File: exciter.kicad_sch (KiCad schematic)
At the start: 37 parts, among them U7 CC1200, X1 40MHz

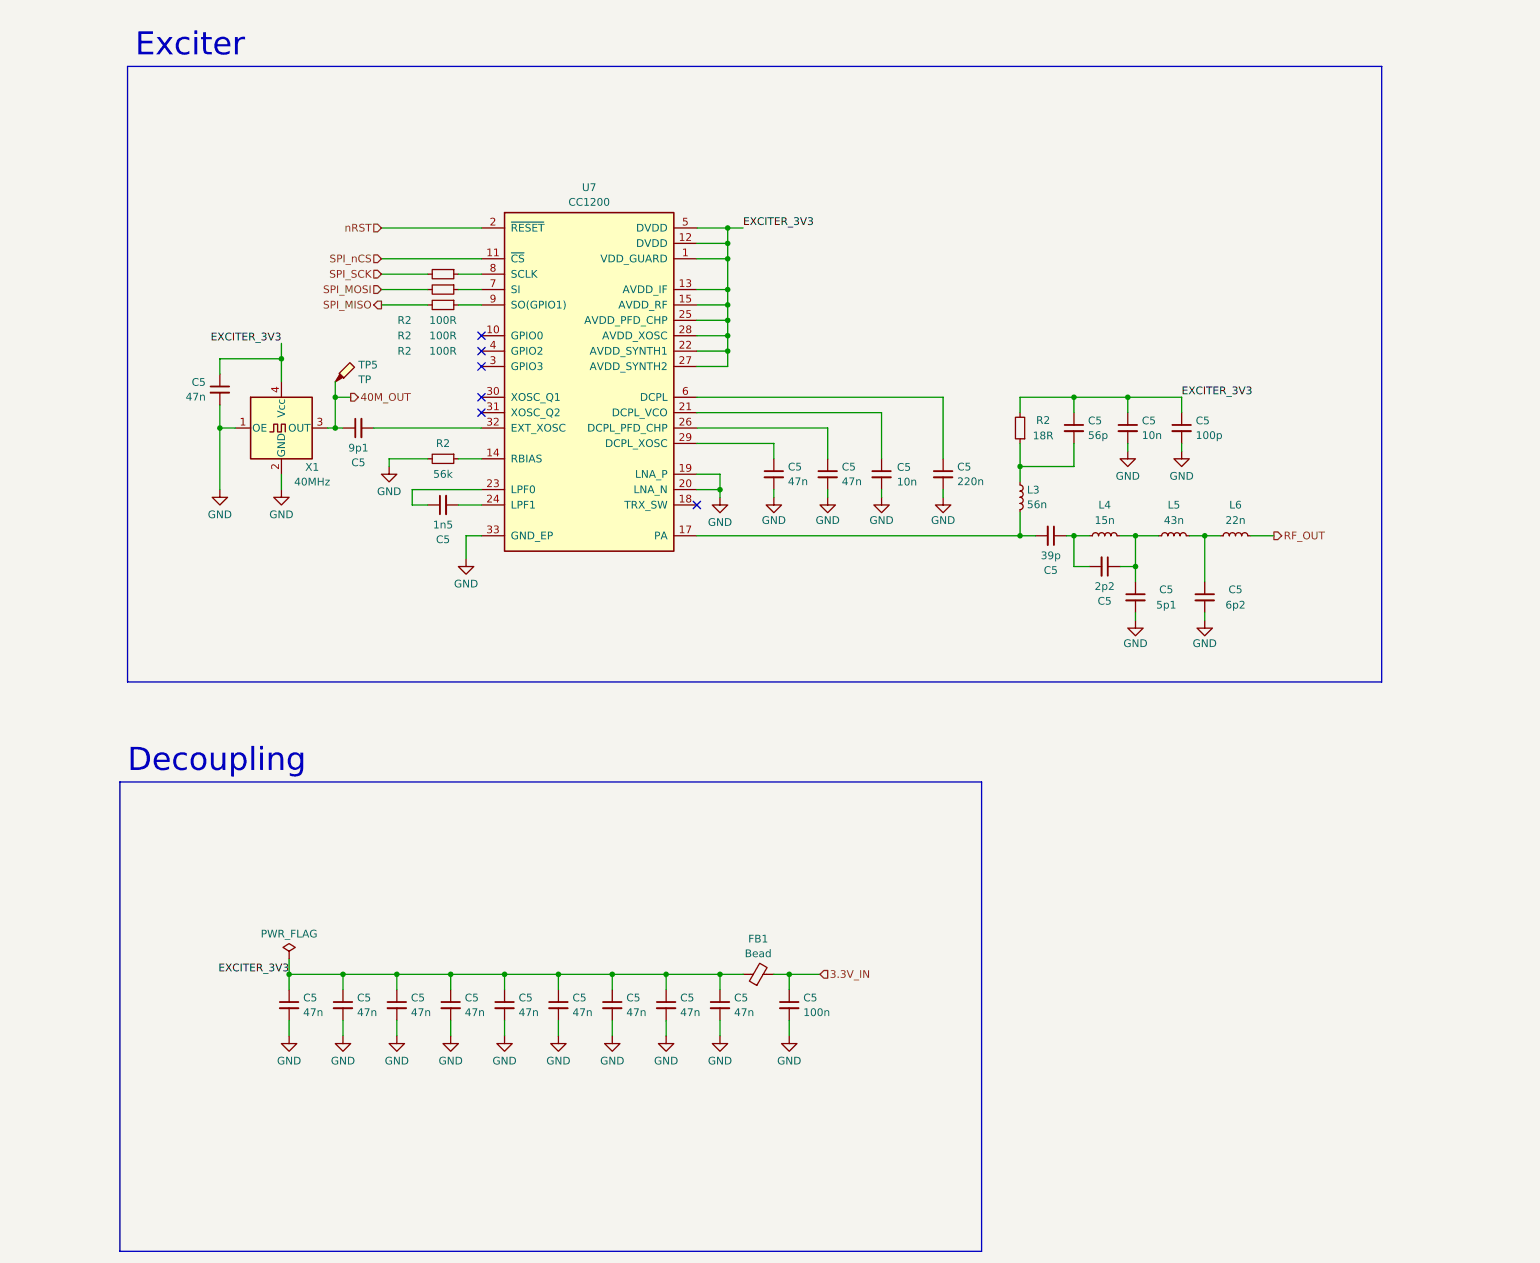
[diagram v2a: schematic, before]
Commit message: WIP rev B
- replaced R44-R46 with 22k
- exposed BOOT0 at the DA15 connector
- added a testpoint at DAC OUT2
- added a buffer to the 40MHz reference oscillator
- removed C2
- bypassed R5 with a 100nF capacitor
- changed D5's voltage to 5.1V
- routed TX_SAMP_CLK
- changed temperature sensor's supply voltage to 5V
- added a series of 100p, 1n and 10n capacitors at PA_VGG
- reduced N-connector cutouts to 2.5mm
- improved RF output track a little
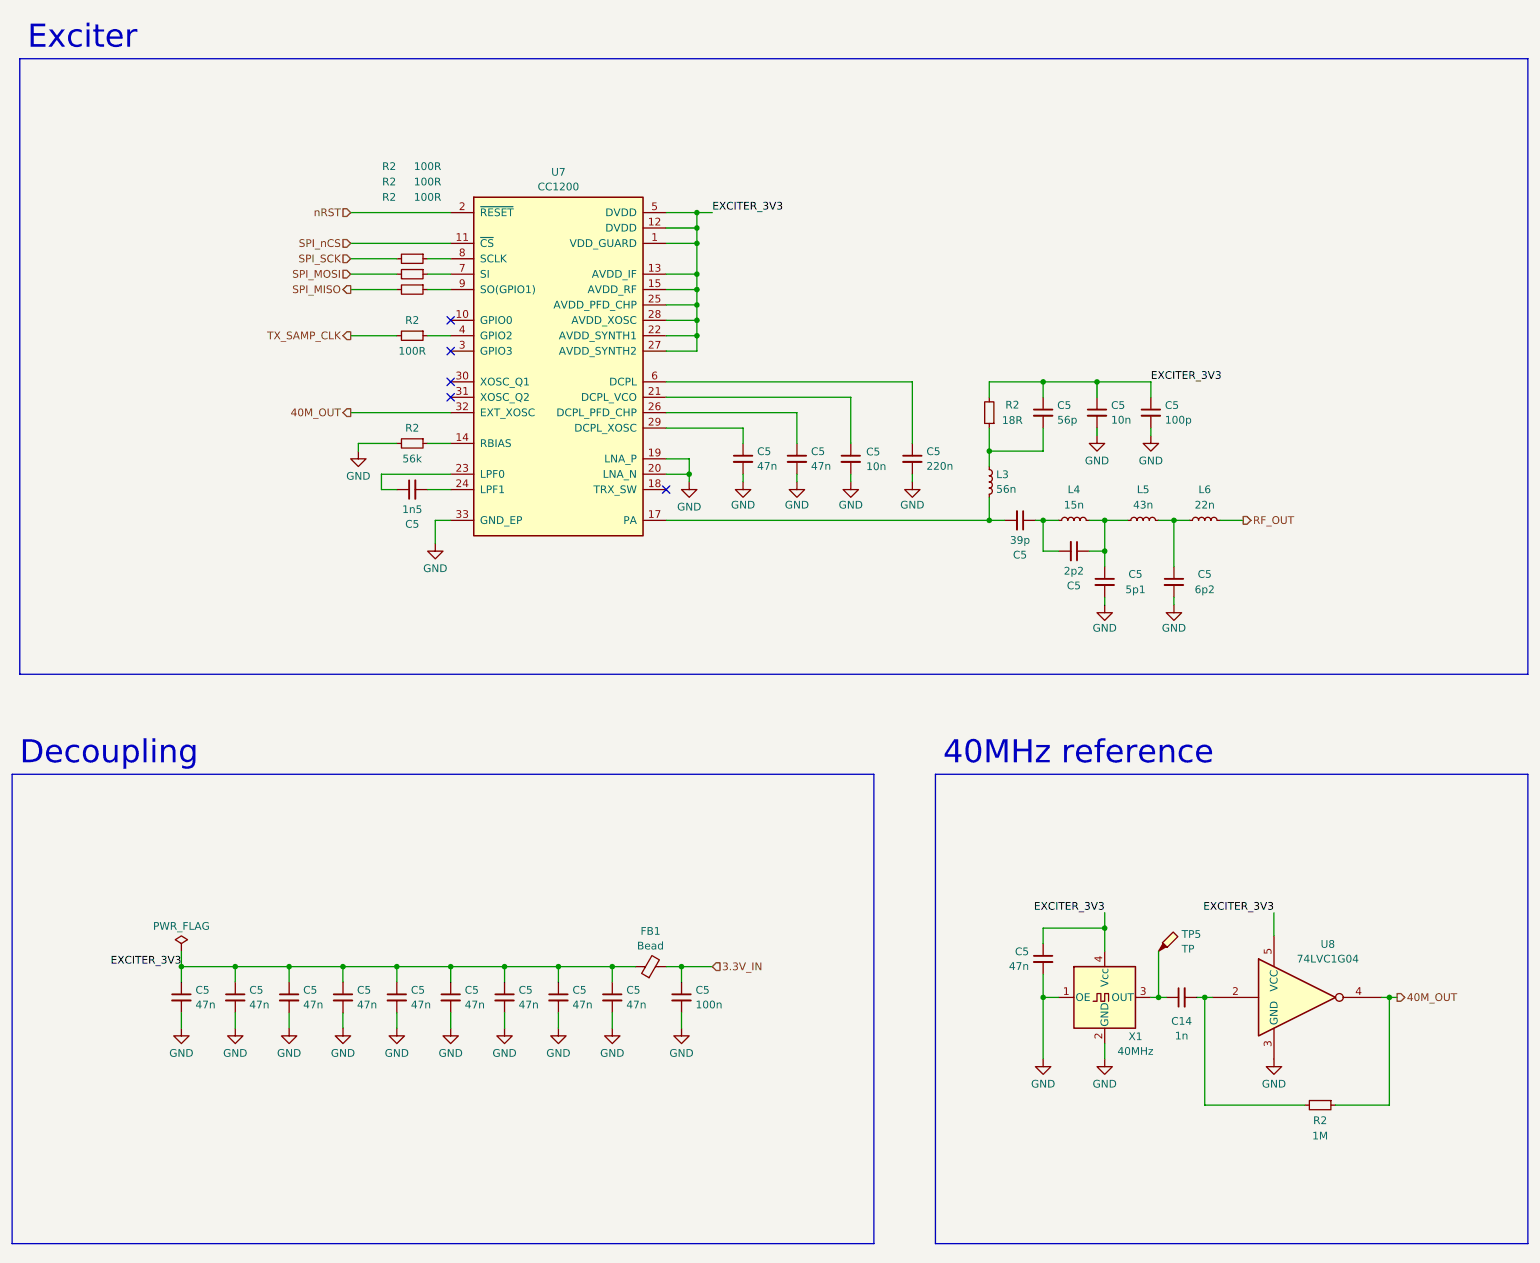
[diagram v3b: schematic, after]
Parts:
- removed C5: 9p1, Capacitor_SMD:C_0603_1608Metric, symbol Device:C_Small
- added C14: 1n, Capacitor_SMD:C_0603_1608Metric, symbol Device:C_Small
- added R2: 100R, Resistor_SMD:R_0603_1608Metric, symbol Device:R_Small
- added R2: 1M, Resistor_SMD:R_0603_1608Metric, symbol Device:R_Small
- added U8: 74LVC1G04, Package_TO_SOT_SMD:SOT-23-5, symbol 74xGxx:74LVC1G04
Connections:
- net 40M_OUT: now also U7.32 (EXT_XOSC), R2.1, U8.4; no longer TP5.1, X1.3 (OUT)
- net EXCITER_3V3: now also U8.5 (VCC)
- net GND: now also U8.3 (GND)
- net at U7.4 (GPIO2): now also R2.1
- new net: C14.1, TP5.1, X1.3 (OUT)
- new net: C14.2, R2.2, U8.2
- new net TX_SAMP_CLK: R2.2
- no-connect marks 6 -> 5
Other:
- note added: "40MHz reference"
- moved on the sheet: C5, FB1, L3, L4, L5, L6, R2, TP5, U7, X1

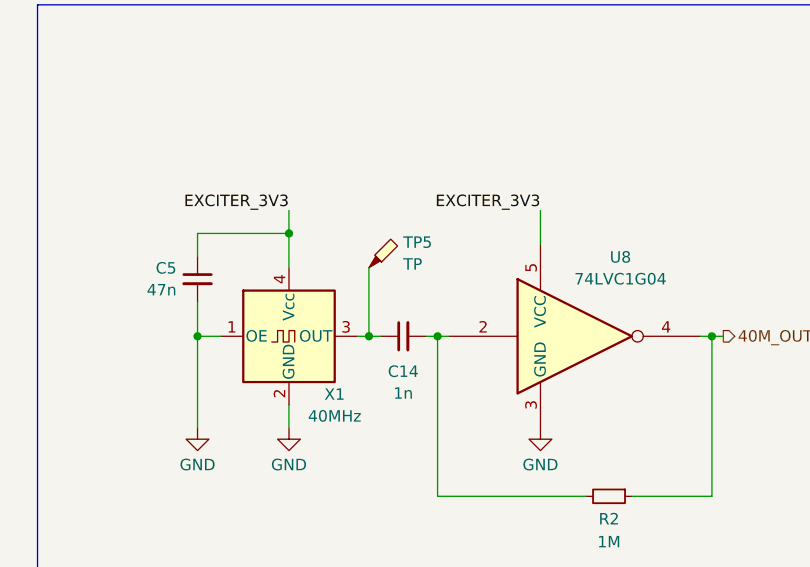
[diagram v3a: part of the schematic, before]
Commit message: routed the 40MHz oscillator
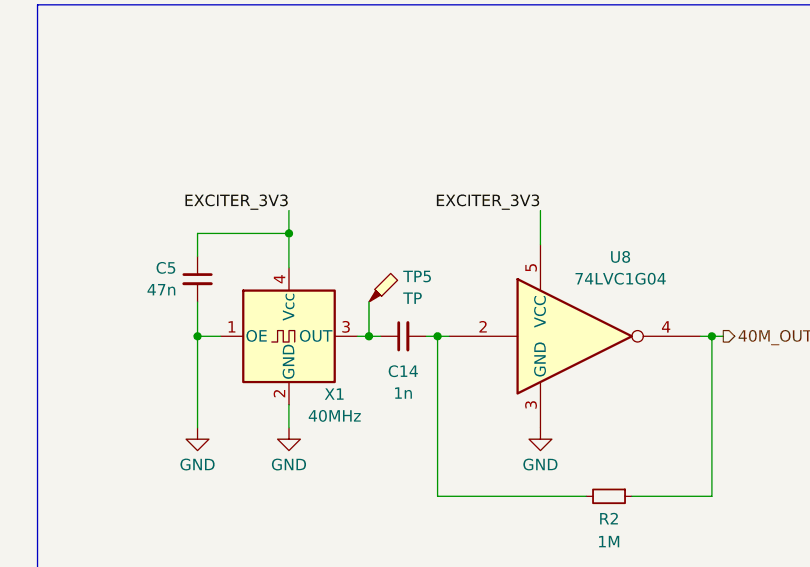
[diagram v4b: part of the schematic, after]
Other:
- moved on the sheet: TP5
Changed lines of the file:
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@@
     (stroke (width 0) (type default))
   )
-  (wire (pts (xy 273.05 195.58) (xy 273.05 203.2))
+  (wire (pts (xy 273.05 199.39) (xy 273.05 203.2))
     (stroke (width 0) (type default))
   )
@@
     )
   )
-  (symbol (lib_id "Connector:TestPoint_Probe") (at 273.05 195.58 0) (unit 1)
+  (symbol (lib_id "Connector:TestPoint_Probe") (at 273.05 199.39 0) (unit 1)
     (in_bom yes) (on_board yes) (dnp no)
-    (property "Reference" "TP5" (at 276.86 192.7804 0)
-      (effects (font (size 1.27 1.27)) (justify left))
-    )
-    (property "Value" "TP" (at 276.86 195.2046 0)
-      (effects (font (size 1.27 1.27)) (justify left))
-    )
-    (property "Footprint" "TestPoint:TestPoint_Pad_D1.5mm" (at 278.13 195.58 0)
-      (effects (font (size 1.27 1.27)) hide)
-    )
-    (property "Datasheet" "~" (at 278.13 195.58 0)
-      (effects (font (size 1.27 1.27)) hide)
-    )
-    (property "PN" "-" (at 273.05 195.58 0)
-      (effects (font (size 1.27 1.27)) hide)
-    )
-    (property "MPN" "-" (at 273.05 195.58 0)
-      (effects (font (size 1.27 1.27)) hide)
-    )
+    (property "Reference" "TP5" (at 276.86 196.5904 0)
+      (effects (font (size 1.27 1.27)) (justify left))
+    )
+    (property "Value" "TP" (at 276.86 199.0146 0)
+      (effects (font (size 1.27 1.27)) (justify left))
+    )
+    (property "Footprint" "TestPoint:TestPoint_Pad_D1.5mm" (at 278.13 199.39 0)
+      (effects (font (size 1.27 1.27)) hide)
+    )
+    (property "Datasheet" "~" (at 278.13 199.39 0)
+      (effects (font (size 1.27 1.27)) hide)
+    )
+    (property "PN" "-" (at 273.05 199.39 0)
+      (effects (font (size 1.27 1.27)) hide)
+    )
+    (property "MPN" "-" (at 273.05 199.39 0)
+      (effects (font (size 1.27 1.27)) hide)
+    )

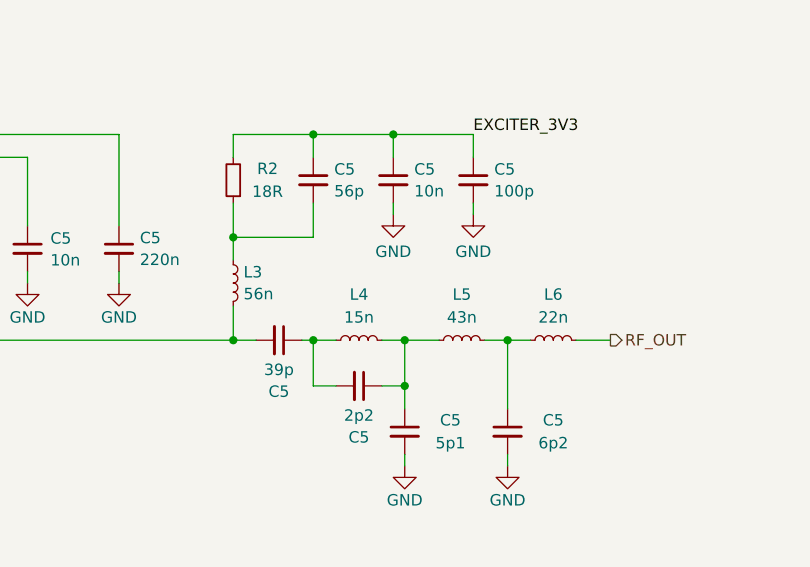
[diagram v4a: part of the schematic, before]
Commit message: WIP rev B
- added bleed resistors
- power supply now uses linear regulators
- routed RX_SAMP_CLK
- added some decoupling at RF_PA_VDD
- added some GND vias here and there
- updated BOM
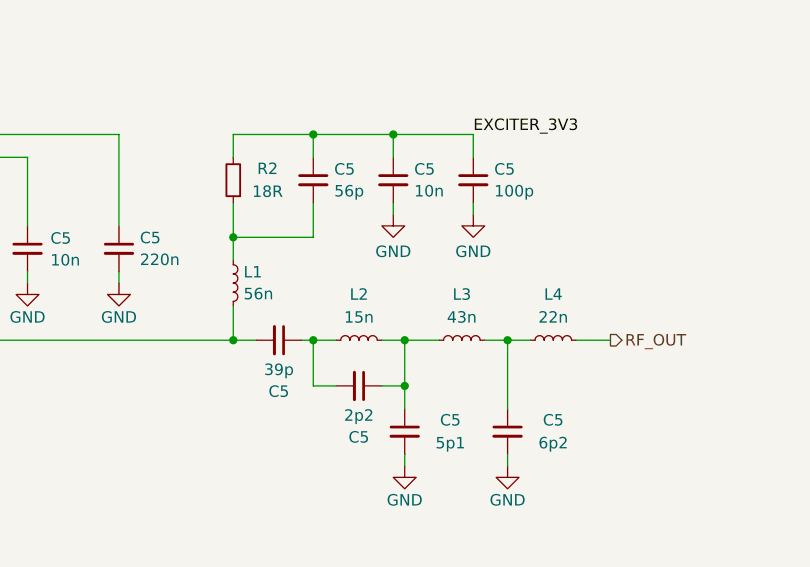
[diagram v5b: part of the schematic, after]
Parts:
- renumbered L3 to L1, L4 to L2, L5 to L3, L6 to L4

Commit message: L1, L6 - PN update
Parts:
- L1: MPN LQW18AS56NG00D -> 81-LQW18AN56NG00D; PN LQW18AS56NG00D -> 81-LQW18AN56NG00D
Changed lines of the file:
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@@
       (effects (font (size 1.27 1.27)) hide)
     )
-    (property "MPN" "LQW18AS56NG00D" (at 245.11 118.11 0)
+    (property "MPN" "81-LQW18AN56NG00D" (at 245.11 118.11 0)
       (effects (font (size 1.27 1.27)) hide)
     )
-    (property "PN" "LQW18AS56NG00D" (at 245.11 118.11 0)
+    (property "PN" "81-LQW18AN56NG00D" (at 245.11 118.11 0)
       (effects (font (size 1.27 1.27)) hide)
     )

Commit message: updated PCB render
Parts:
- R2: MPN 71-CRCW06031M00FKEB -> 71-CRCW06031M00FKEB; PN 71-CRCW06031M00FKEB -> 71-CRCW06031M00FKEB
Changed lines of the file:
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@@
       (effects (font (size 1.27 1.27)) hide)
     )
-    (property "PN" "71-CRCW06031M00FKEB " (at 299.72 220.98 0)
+    (property "PN" "71-CRCW06031M00FKEB" (at 299.72 220.98 0)
       (effects (font (size 1.27 1.27)) hide)
     )
-    (property "MPN" "71-CRCW06031M00FKEB " (at 299.72 220.98 0)
+    (property "MPN" "71-CRCW06031M00FKEB" (at 299.72 220.98 0)
       (effects (font (size 1.27 1.27)) hide)
     )
